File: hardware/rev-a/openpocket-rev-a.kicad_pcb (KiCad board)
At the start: 8 copper layers, 115 x 72 mm, 309 parts, among them J1 ER-TFT050A3-2 FFC, J11 5.8 GHz antenna U.FL, J12 push-push microSD, J13 speaker solder pads, J14 SSD1306 128x64 OLED pads, J15 expander developer pads, J16 controls ground pads, J2 USB-C, J3 battery/NTC, J4 speaker connector, J5 master switch, J6 ELRS, J7 left gimbal, J8 right gimbal, J9 controls, Q1 dual protection FET, Q2 Q_BUZZ buzzer MOSFET, U1 ESP32-S3-MINI-1U-N8, U10 display 3V3 buck, U11 analog OSD, U12 OSD 3V3-to-5V, U13 OSD 5V-to-3V3, U14 CVBS TFT controller, U15 AMT boot flash, U16 AMT flash mux, U17 backlight boost, U18 GPIO expander 0x20, U19 GPIO expander 0x21, U2 1S charger/power path, U20 master load switch, U21 I2S speaker amplifier, U22 3V3_SD load switch, U3 1S protector, U4 fuel gauge, U5 3V3 buck-boost, U6 5V boost, U7 5V_VIDEO load switch, U8 5V_DISPLAY load switch, U9 5V_ELRS load switch, Y1 27.000MHz, Y2 27.000MHz

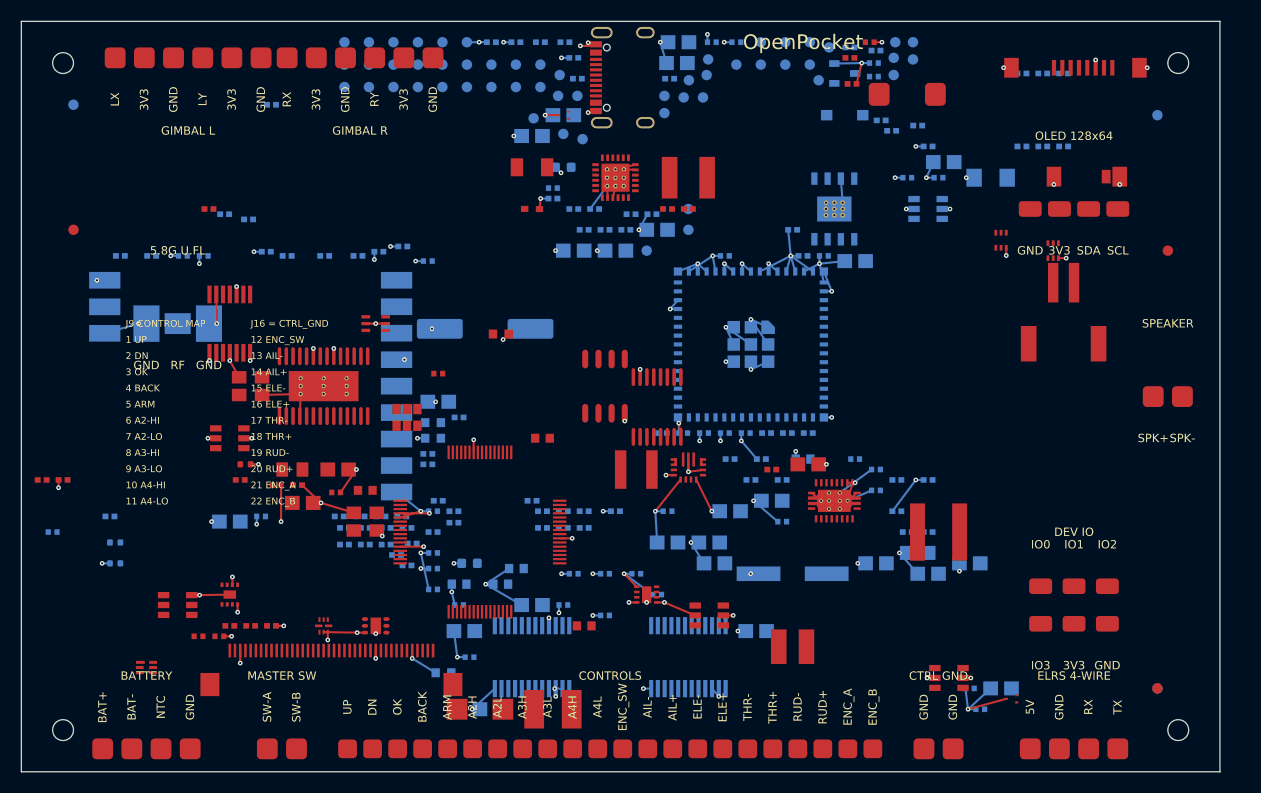
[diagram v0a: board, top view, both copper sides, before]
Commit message: feat(rev-a): add deterministic placement optimizer
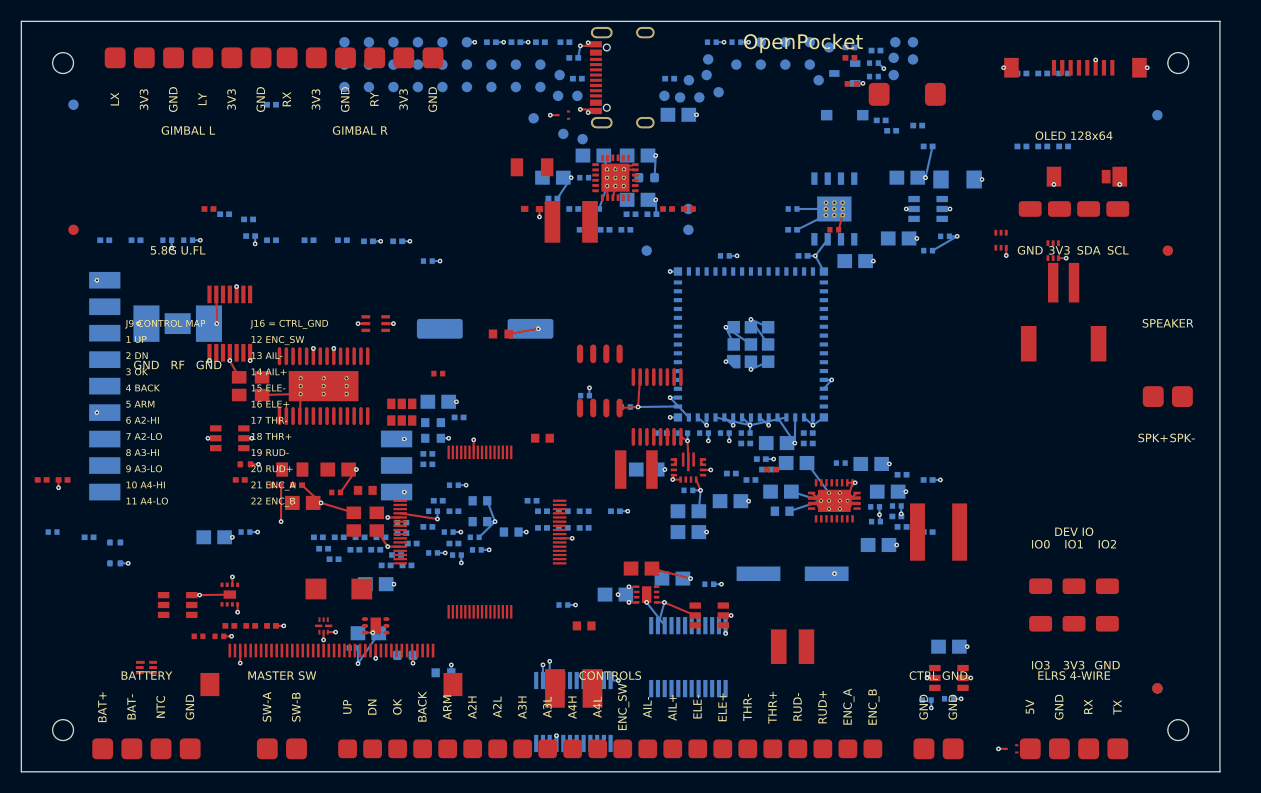
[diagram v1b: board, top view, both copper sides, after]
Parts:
- moved C19 51.3 mm to (57.0, 55.0), turned to 0 degrees
- moved C18 25.5 mm to (85.0, 15.0), turned to 0 degrees
- moved C73 22.1 mm to (41.5, 44.5), turned to 0 degrees
- moved C50 21.8 mm to (72.5, 40.5), turned to 0 degrees
- moved C52 18.9 mm to (59.5, 52.5)
- moved C46 18.4 mm to (83.1, 45.1), turned to 0 degrees
- moved C17 18.3 mm to (78.0, 20.0)
- moved D1 17.8 mm to (30.5, 54.5)
- moved C70 17.1 mm to (54.1, 35.9), turned to 0 degrees
- moved C49 16.5 mm to (74.4, 42.4), turned to 0 degrees
- moved C56 16.3 mm to (34.0, 54.0), turned to 0 degrees
- moved C71 16.1 mm to (58.0, 37.0), turned to 0 degrees
- moved C45 15.8 mm to (82.2, 50.2), turned to 0 degrees
- moved C72 15.5 mm to (43.7, 50.7), turned to 0 degrees
- moved C48 14.4 mm to (72.9, 45.1), turned to 0 degrees
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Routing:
- net GND: track 291.3 -> 269.7 mm, vias 139 -> 147

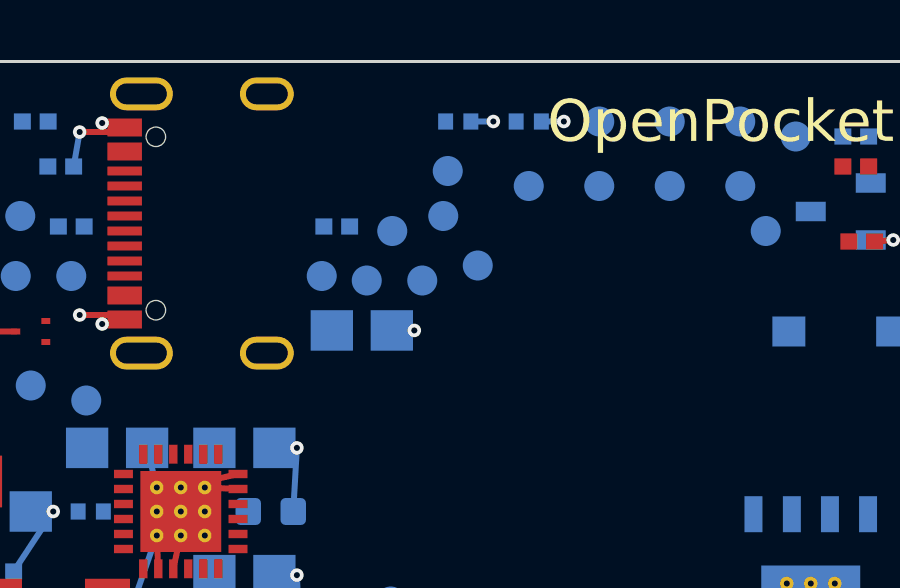
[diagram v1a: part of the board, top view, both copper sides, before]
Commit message: fix(rev-a): remove dangling ELRS debug labels and refresh renders
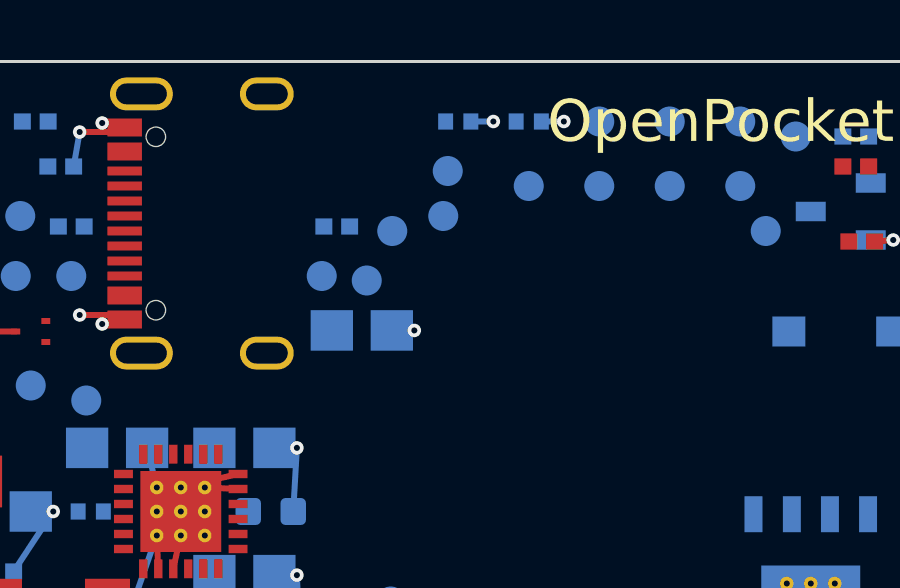
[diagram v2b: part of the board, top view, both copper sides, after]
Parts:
- removed TP54: ESP_BOOT test pad, TEST-PAD-1.0MM
- removed TP55: ESP_EN test pad, TEST-PAD-1.0MM
- TP22: value ELRS_BOOT test pad -> SYS_ALWAYS test pad
- TP23: value ELRS_RESET test pad -> SYS_SWITCHED test pad
- TP24: value SYS_ALWAYS test pad -> POWER_GOOD test pad
- TP25: value SYS_SWITCHED test pad -> 3V3_LOGIC test pad
- TP26: value POWER_GOOD test pad -> SYS_SWITCHED_5V test pad
- TP27: value 3V3_LOGIC test pad -> 5V_VIDEO test pad
- TP28: value SYS_SWITCHED_5V test pad -> 5V_DISPLAY test pad
- TP29: value 5V_VIDEO test pad -> 5V_ELRS test pad
- TP30: value 5V_DISPLAY test pad -> DISPLAY_3V3 test pad
- TP31: value 5V_ELRS test pad -> PANEL_3V3 test pad
- TP32: value DISPLAY_3V3 test pad -> VBUS_USB test pad
- TP33: value PANEL_3V3 test pad -> BAT_RAW test pad
- TP34: value VBUS_USB test pad -> RX_RSSI_RAW test pad
- TP35: value BAT_RAW test pad -> VRX_VIDEO_RAW test pad
- TP36: value RX_RSSI_RAW test pad -> OSD_VIDEO_RAW test pad
- TP37: value VRX_VIDEO_RAW test pad -> AMT_RESET test pad
- TP38: value OSD_VIDEO_RAW test pad -> AMT_FLASH_CS test pad
- TP39: value AMT_RESET test pad -> AMT_FLASH_CLK test pad
- TP40: value AMT_FLASH_CS test pad -> AMT_FLASH_MOSI test pad
- TP41: value AMT_FLASH_CLK test pad -> AMT_FLASH_MISO test pad
- TP42: value AMT_FLASH_MOSI test pad -> BUZZER_PWM test pad
- TP43: value AMT_FLASH_MISO test pad -> BUZZER_LOW test pad
- TP44: value BUZZER_PWM test pad -> AUDIO_I2S_BCLK test pad
- TP45: value BUZZER_LOW test pad -> AUDIO_I2S_WS test pad
- TP46: value AUDIO_I2S_BCLK test pad -> AUDIO_I2S_DATA test pad
- TP47: value AUDIO_I2S_WS test pad -> AUDIO_ENABLE test pad
- TP48: value AUDIO_I2S_DATA test pad -> SPK+ test pad
- TP49: value AUDIO_ENABLE test pad -> SPK- test pad
- TP50: value SPK+ test pad -> BL_LED_A test pad
- TP51: value SPK- test pad -> BL_LED_K test pad
- TP52: value BL_LED_A test pad -> ESP_BOOT test pad
- TP53: value BL_LED_K test pad -> ESP_EN test pad
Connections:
- TP22 pad 1: ELRS_BOOT -> SYS_ALWAYS
- TP23 pad 1: ELRS_RESET -> SYS_SWITCHED
- TP24 pad 1: SYS_ALWAYS -> POWER_GOOD
- TP25 pad 1: SYS_SWITCHED -> 3V3_LOGIC
- TP26 pad 1: POWER_GOOD -> SYS_SWITCHED_5V
- TP27 pad 1: 3V3_LOGIC -> 5V_VIDEO
- TP28 pad 1: SYS_SWITCHED_5V -> 5V_DISPLAY
- TP29 pad 1: 5V_VIDEO -> 5V_ELRS
- TP30 pad 1: 5V_DISPLAY -> DISPLAY_3V3
- TP31 pad 1: 5V_ELRS -> PANEL_3V3
- TP32 pad 1: DISPLAY_3V3 -> VBUS_USB
- TP33 pad 1: PANEL_3V3 -> BAT_RAW
- TP34 pad 1: VBUS_USB -> RX_RSSI_RAW
- TP35 pad 1: BAT_RAW -> VRX_VIDEO_RAW
- TP36 pad 1: RX_RSSI_RAW -> OSD_VIDEO_RAW
- TP37 pad 1: VRX_VIDEO_RAW -> AMT_RESET
- TP38 pad 1: OSD_VIDEO_RAW -> AMT_FLASH_CS
- TP39 pad 1: AMT_RESET -> AMT_FLASH_CLK
- TP40 pad 1: AMT_FLASH_CS -> AMT_FLASH_MOSI
- TP41 pad 1: AMT_FLASH_CLK -> AMT_FLASH_MISO
- TP42 pad 1: AMT_FLASH_MOSI -> BUZZER_PWM
- TP43 pad 1: AMT_FLASH_MISO -> BUZZER_LOW
- TP44 pad 1: BUZZER_PWM -> AUDIO_I2S_BCLK
- TP45 pad 1: BUZZER_LOW -> AUDIO_I2S_WS
- TP46 pad 1: AUDIO_I2S_BCLK -> AUDIO_I2S_DATA
- TP47 pad 1: AUDIO_I2S_WS -> AUDIO_ENABLE
- TP48 pad 1: AUDIO_I2S_DATA -> SPK+
- TP49 pad 1: AUDIO_ENABLE -> SPK-
- TP50 pad 1: SPK+ -> BL_LED_A
- TP51 pad 1: SPK- -> BL_LED_K
- TP52 pad 1: BL_LED_A -> ESP_BOOT
- TP53 pad 1: BL_LED_K -> ESP_EN

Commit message: feat(rev-a): add edge ground pads for controls
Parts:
- added J17: right control ground pads, GROUND-EDGE-11, F.Cu at (111.0, 51.0)
- J16: value controls ground pads -> left control ground pads; footprint EDGE-PADS-2 -> GROUND-EDGE-11
- moved J16 86.1 mm to (4.00, 51.0)
- moved R56 6.36 mm to (6.50, 39.5)
- moved R57 3.54 mm to (6.50, 41.5)
- moved TVS1 1.58 mm to (47.5, 18.5)
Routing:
- net GND: track 269.7 -> 280.9 mm, vias 147 -> 155
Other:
- board text added: "CTRL GND LEFT"
- board text added: "CTRL GND RIGHT"
- board text added: "J16/J17 = CTRL_GND"
- board text removed: "CTRL GND"
- board text removed: "J16 = CTRL_GND"

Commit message: fix(rev-a): place UFL beside RX5808 RF pad
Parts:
- moved J11 28.5 mm to (40.0, 42.6), turned to 90 degrees
- moved C73 5.00 mm to (46.5, 44.5)
- moved R10 4.72 mm to (43.5, 36.0)
- moved R11 4.72 mm to (43.5, 37.5)
- moved R12 4.72 mm to (43.0, 39.0)
- moved R58 4.27 mm to (43.0, 41.0)
- moved R77 3.54 mm to (44.0, 44.5)
- moved R86 2.55 mm to (33.5, 51.7)
- moved R53 2.24 mm to (43.0, 40.0)
- moved R76 2.06 mm to (40.5, 48.0)
- moved C15 1.41 mm to (38.5, 48.0)
- moved R18 1.00 mm to (39.0, 49.5)
- moved R82 0.71 mm to (37.0, 50.6)
- moved R87 0.71 mm to (35.5, 51.7)
- moved R88 0.71 mm to (37.5, 51.7)
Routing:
- net GND: track 280.9 -> 284.9 mm, vias 155 -> 154

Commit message: feat(rev-a): split controls into edge solder groups
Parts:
- removed the J14 at (101.0, 18.0)
- removed J16: left control ground pads, GROUND-EDGE-11
- removed J17: right control ground pads, GROUND-EDGE-11
- added J18: rotary encoder control pads, ENCODER-CONTROL-PADS, F.Cu at (4.00, 50.0)
- added J19: ARM switch pads, ARM-CONTROL-PADS, F.Cu at (111.0, 22.0)
- added J20: AUX2 three-position switch pads, AUX2-CONTROL-PADS, F.Cu at (111.0, 28.0)
- added J21: AUX3 three-position switch pads, AUX3-CONTROL-PADS, F.Cu at (111.0, 32.0)
- added J22: AUX4 three-position switch pads, AUX4-CONTROL-PADS, F.Cu at (111.0, 46.0)
- added J23: AIL trim pads, AIL-TRIM-PADS, F.Cu at (111.0, 52.0)
- added J24: ELE trim pads, ELE-TRIM-PADS, F.Cu at (111.0, 60.0)
- added J25: THR trim pads, THR-TRIM-PADS, F.Cu at (4.00, 57.0)
- added J26: RUD trim pads, RUD-TRIM-PADS, F.Cu at (4.00, 64.0)
- added U22: 3V3_SD load switch, SOT-23-6_L2.9-W1.6-P0.95-LS2.8-BR, B.Cu at (87.0, 18.0)
- J14: renamed from U22; value 3V3_SD load switch -> SSD1306 128x64 OLED pads; footprint SOT-23-6_L2.9-W1.6-P0.95-LS2.8-BR -> DEV-PADS-4; moved to F.Cu
- J9: value controls -> menu/UI control pads; footprint EDGE-PADS-22 -> MENU-CONTROL-PADS
- moved J9 76.6 mm to (4.00, 14.0)
- moved J15 28.6 mm to (75.0, 68.0)
- moved J14 21.0 mm to (108.0, 18.0)
- moved FID2 20.0 mm to (90.0, 22.0)
- moved FID1 11.0 mm to (16.0, 20.0)
- moved FID4 11.0 mm to (16.0, 8.00)
- moved FID5 11.0 mm to (98.0, 9.00)
- moved FID6 11.0 mm to (98.0, 64.0)
- moved FID3 9.00 mm to (100.0, 64.0)
- moved R56 6.36 mm to (2.00, 44.0)
- moved R59 4.95 mm to (3.00, 46.0)
- moved J13 4.00 mm to (110.0, 40.0)
- moved R62 3.91 mm to (12.0, 47.5)
- moved R57 3.54 mm to (4.00, 44.0)
- moved R63 2.83 mm to (7.00, 54.0)
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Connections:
- J14 pad 1: 3V3_LOGIC -> GND
- J14 pad 2: GND -> 3V3_LOGIC
- J14 pad 3: EN_3V3_SD -> I2C_SDA
- J14 pad 4: 3V3_SD_CT -> I2C_SCL
- J9 pad 1: CTRL_0_0 -> GND
- J9 pad 2: CTRL_0_1 -> CTRL_0_0
- J9 pad 3: CTRL_0_2 -> GND
- J9 pad 4: CTRL_0_3 -> CTRL_0_1
- J9 pad 5: CTRL_0_4 -> GND
- J9 pad 6: CTRL_0_5 -> CTRL_0_2
- J9 pad 7: CTRL_0_6 -> GND
- J9 pad 8: CTRL_0_7 -> CTRL_0_3
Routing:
- net GND: track 284.9 -> 275.1 mm, vias 154 -> 145
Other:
- board text removed: "1 UP"
- board text removed: "10 A4-HI"
- board text removed: "11 A4-LO"
- board text removed: "12 ENC_SW"
- board text removed: "13 AIL-"
- board text removed: "14 AIL+"
- board text removed: "15 ELE-"
- board text removed: "16 ELE+"
- board text removed: "17 THR-"
- board text removed: "18 THR+"
- board text removed: "19 RUD-"
- board text removed: "2 DN"
- board text removed: "20 RUD+"
- board text removed: "21 ENC_A"
- board text removed: "22 ENC_B"
- board text removed: "3 OK"
- board text removed: "4 BACK"
- board text removed: "5 ARM"
- board text removed: "6 A2-HI"
- board text removed: "7 A2-LO"
- board text removed: "8 A3-HI"
- board text removed: "9 A3-LO"
- board text removed: "A2H"
- board text removed: "A2L"
- board text removed: "A3H"
- board text removed: "A3L"
- board text removed: "A4H"
- board text removed: "A4L"
- board text removed: "AIL+"
- board text removed: "AIL-"
- board text removed: "ARM"
- board text removed: "BACK"
- board text removed: "CONTROLS"
- board text removed: "CTRL GND LEFT"
- board text removed: "CTRL GND RIGHT"
- board text removed: "DN"
- board text removed: "ELE+"
- board text removed: "ELE-"
- board text removed: "ENC_A"
- board text removed: "ENC_B"
- board text removed: "ENC_SW"
- board text removed: "J16/J17 = CTRL_GND"
- board text removed: "J9 CONTROL MAP"
- board text removed: "OK"
- board text removed: "RUD+"
- board text removed: "RUD-"
- board text removed: "THR+"
- board text removed: "THR-"
- board text removed: "UP"

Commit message: fix(rev-a): unify user control solder pads
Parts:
- moved R59 4.95 mm to (6.50, 49.5)
- moved R62 3.91 mm to (9.00, 50.0)
- moved R63 2.83 mm to (9.00, 52.0)
- moved C67 1.41 mm to (3.00, 49.0)
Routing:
- net GND: track 275.1 -> 273.7 mm, vias 145 -> 146

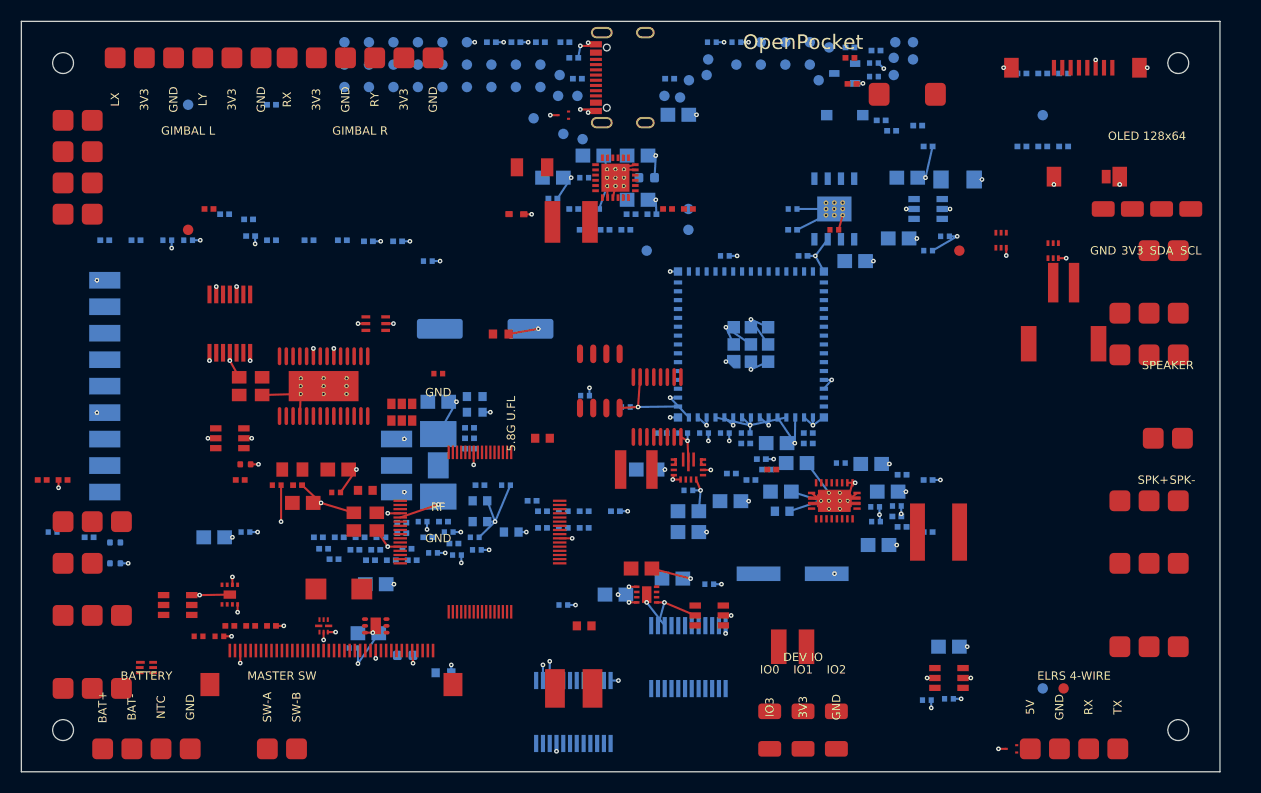
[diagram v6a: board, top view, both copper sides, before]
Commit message: feat(rev-a): apply legal power-video placement optimization
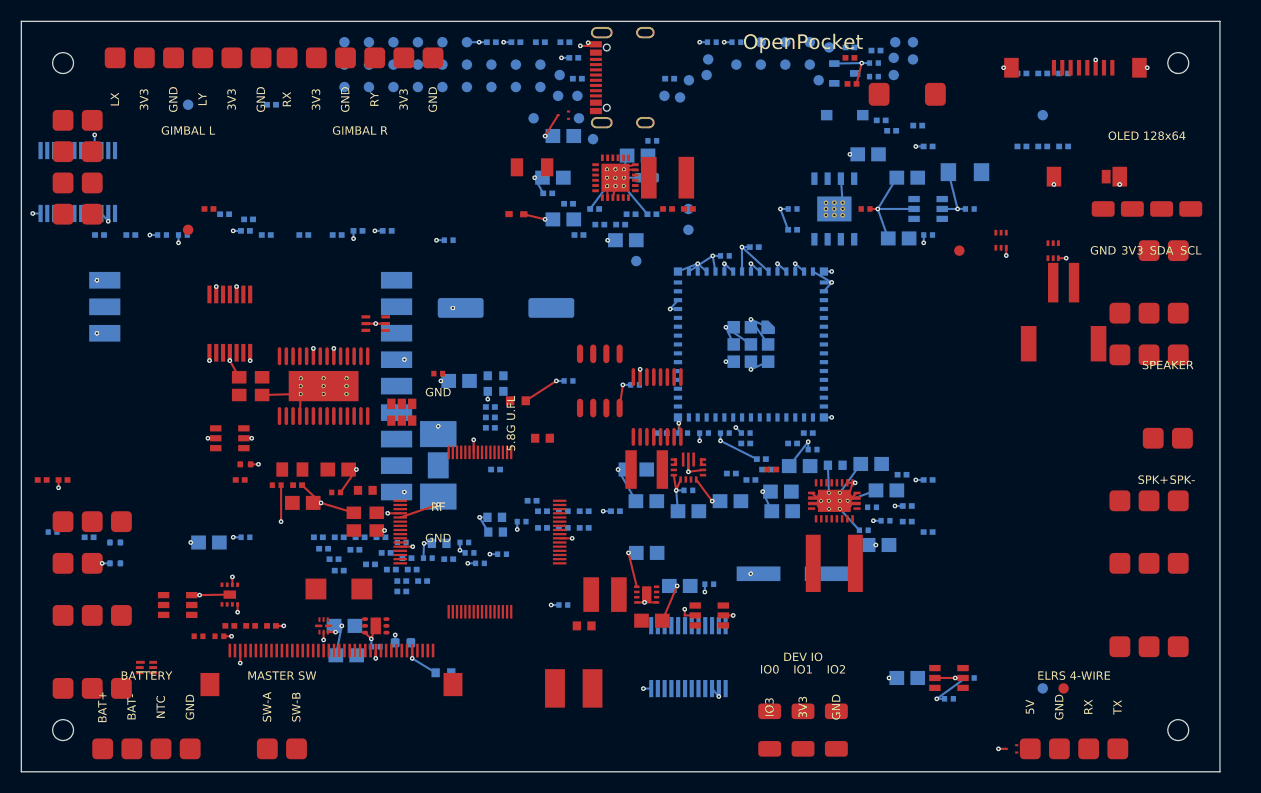
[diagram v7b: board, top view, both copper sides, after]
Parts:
- moved U18 69.6 mm to (5.41, 15.4), turned to 180 degrees
- moved L5 18.7 mm to (56.0, 55.0)
- moved C50 13.8 mm to (82.2, 50.2), turned to 180 degrees
- moved C45 10.7 mm to (72.9, 45.1), turned to 180 degrees
- moved L3 10.4 mm to (78.0, 52.0)
- moved C21 10.3 mm to (81.2, 12.8), turned to 180 degrees
- moved L1 10.2 mm to (62.0, 15.0)
- moved C42 8.14 mm to (75.9, 41.1), turned to 180 degrees
- moved C30 7.43 mm to (60.5, 11.5), turned to 180 degrees
- moved C56 7.39 mm to (31.2, 60.8), turned to 180 degrees
- moved C28 7.36 mm to (52.0, 11.0), turned to 180 degrees
- moved C31 6.76 mm to (52.0, 19.0), turned to 180 degrees
- moved C40 6.73 mm to (78.1, 42.6), turned to 180 degrees
- moved R103 6.61 mm to (47.6, 36.4)
- moved R76 6.26 mm to (35.0, 51.0), turned to 180 degrees
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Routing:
- net GND: track 273.7 -> 283.2 mm, vias 146 -> 133
